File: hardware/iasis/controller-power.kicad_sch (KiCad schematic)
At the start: 10 parts, among them U1181 74HC595D,118, U1182 74HC595D,118

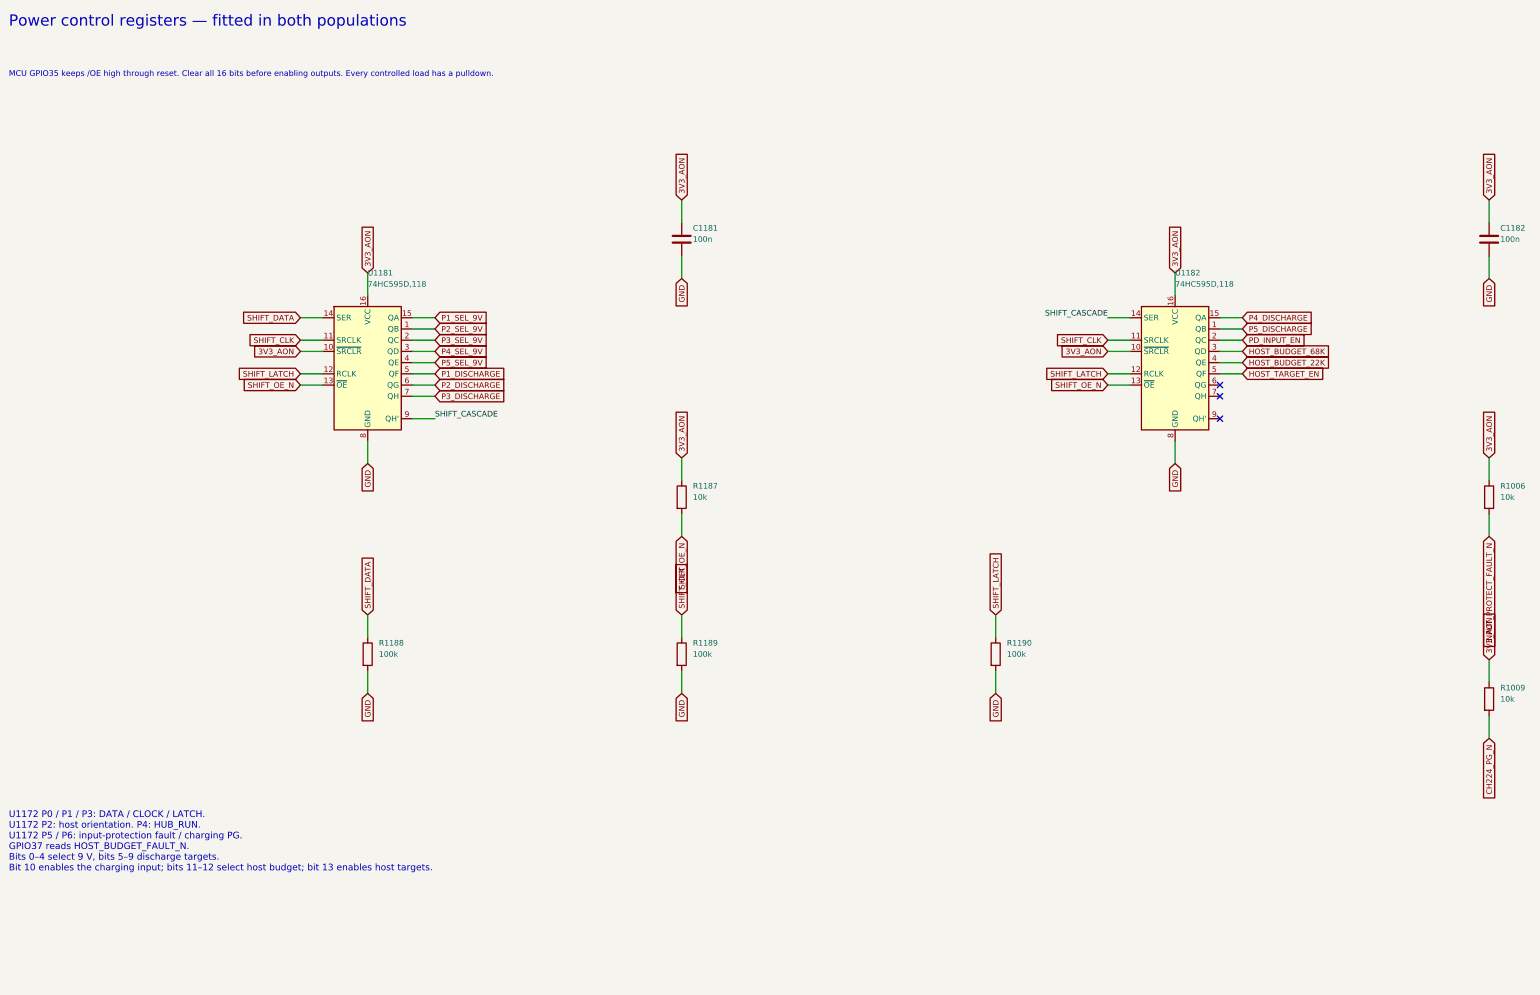
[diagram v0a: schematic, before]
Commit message: Wire the schematic islands and side-match the RP2354 GPIOs
Each sheet now draws its circuits with wires. Labels remain at block edges
and on single-part islands: buttons, test points, decoupling and pull
resistors. The target-port page wires its hierarchical labels straight to
the child sheet pins, the ports page points its labels away from each
block, and the root sheet keeps every block clear of the title block.

The RP2354B GPIOs are reassigned so each signal leaves the package on the
side facing its destination. Update PCB from Schematic applied the 43
U1101 pad-net changes with no geometry change. Otherwise the netlist
matches the previous design, ERC keeps its 14 existing warnings and DRC
reports no parity issues.
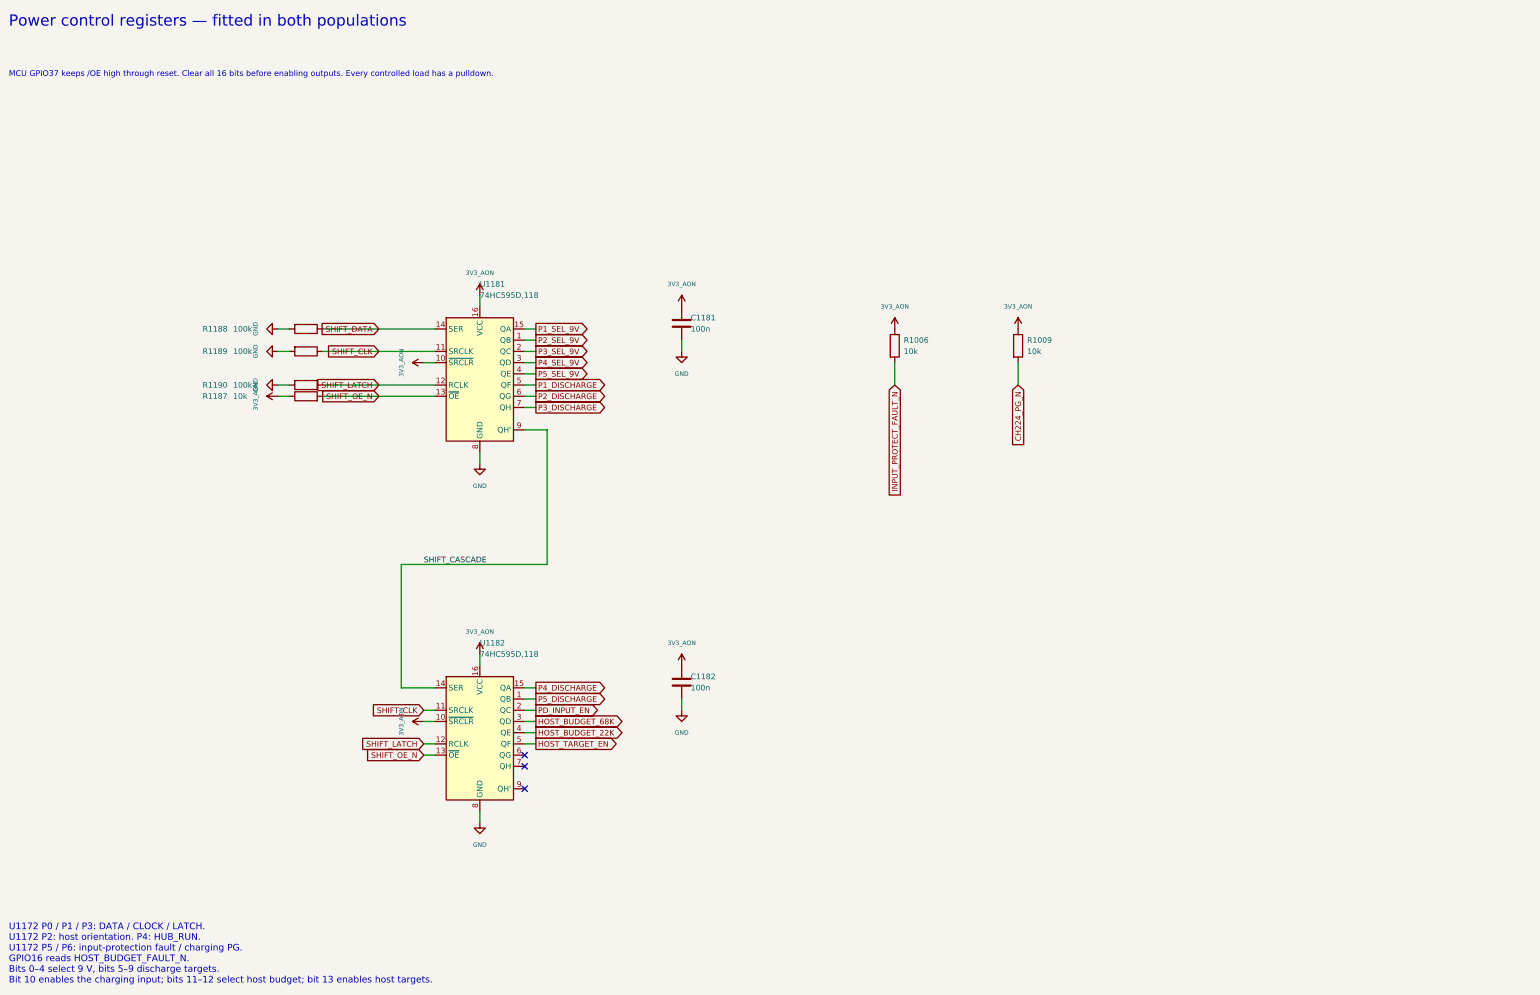
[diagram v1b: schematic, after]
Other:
- note added: "MCU GPIO37 keeps /OE high through reset. Clear all 16 bits before enabling outputs. Every controlled load has a pulldown."
- note added: "U1172 P0 / P1 / P3: DATA / CLOCK / LATCH. U1172 P2: host orientation. P4: HUB_RUN. U1172 P5 / P6: input-protection fault / charging PG. GPIO16 reads HOST_BUDGET_FAULT_N. Bits 0–4 select 9 V, bits 5–9 discharge targets. Bit 10 enables the charging input; bits 11–12 select host budget; bit 13 enables host targets."
- note removed: "MCU GPIO35 keeps /OE high through reset. Clear all 16 bits before enabling outputs. Every controlled load has a pulldown."
- note removed: "U1172 P0 / P1 / P3: DATA / CLOCK / LATCH. U1172 P2: host orientation. P4: HUB_RUN. U1172 P5 / P6: input-protection fault / charging PG. GPIO37 reads HOST_BUDGET_FAULT_N. Bits 0–4 select 9 V, bits 5–9 discharge targets. Bit 10 enables the charging input; bits 11–12 select host budget; bit 13 enables host targets."
- moved on the sheet: C1181, C1182, R1006, R1009, R1187, R1188, R1189, R1190, U1181, U1182

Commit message: Redraw the controller support sheets
The management bus, indicator, power-control, voltage-measurement and
temperature sheets read left to right, with supplies up, ground down
and decoupling beside each IC. Pull resistors, test points and buttons
are labelled islands; everything else is wired. Supply rails use power
symbols with their existing net names, fields sit clear of bodies,
wires and text, and each sheet carries a title, date and revision. The
netlist is unchanged.
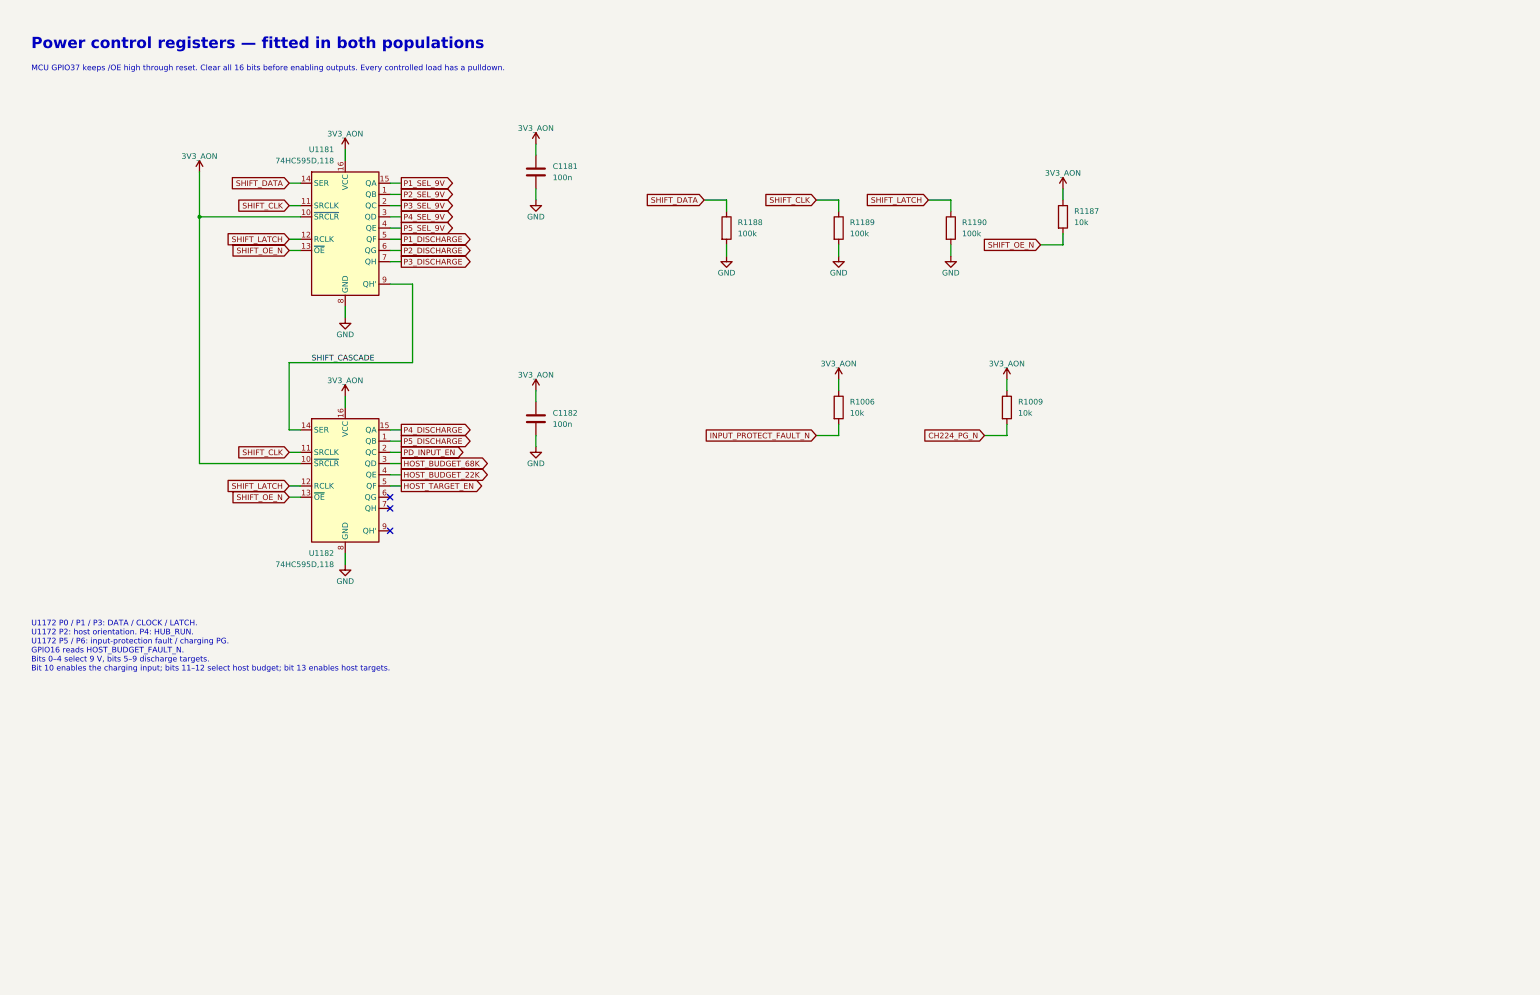
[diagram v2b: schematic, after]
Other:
- title: (none) -> Power control registers
- moved on the sheet: C1181, C1182, R1006, R1009, R1187, R1188, R1189, R1190, U1181, U1182
